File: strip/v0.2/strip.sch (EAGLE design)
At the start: 97 parts, among them IC1 LP2992, IC2 AUIRS2184S, IC3 MAX3051, IC5 AUIRS2184S, IC6 AUIRS2184S, IC7 STM32F050CX, Q1 IRF7828, Q2 IRF7828, Q3 IRF7828, Q4 IRF7828, Q5 IRF7828, Q6 IRF7828, U1 INA214AIDCKT

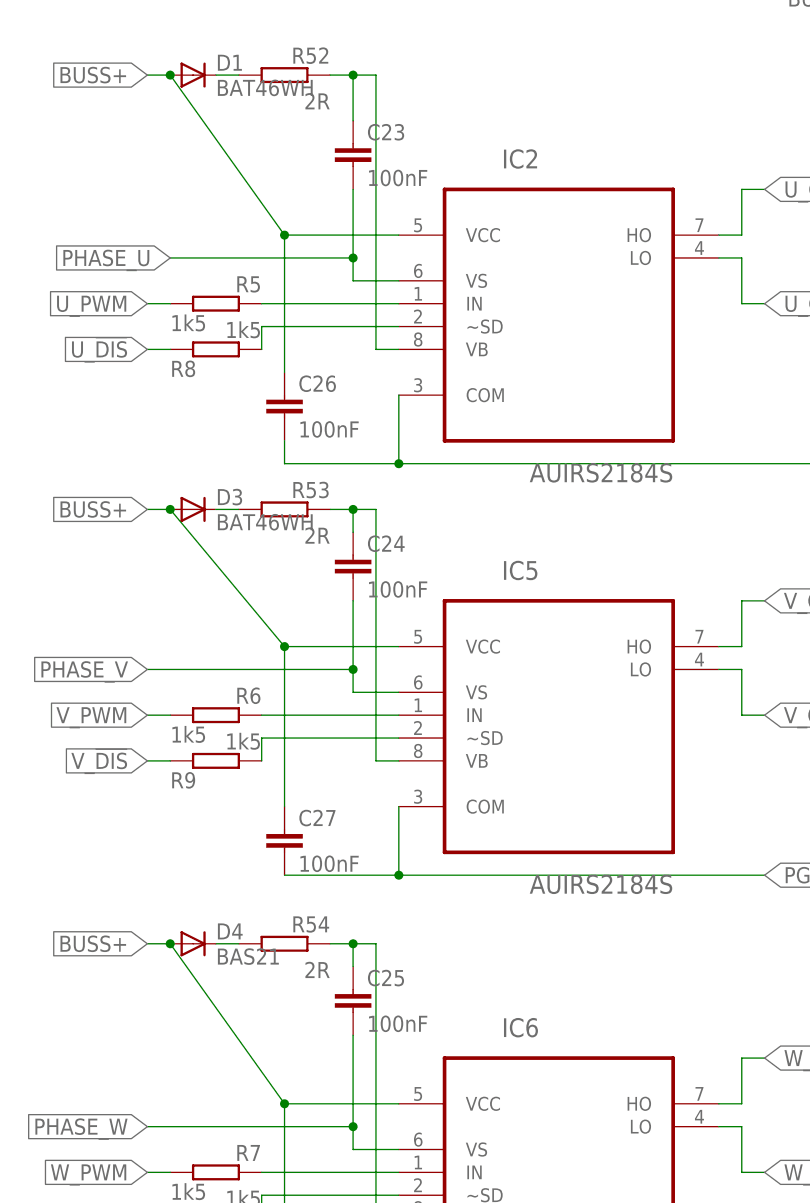
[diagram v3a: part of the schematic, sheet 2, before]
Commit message: Wired the layout of the new current measurement.
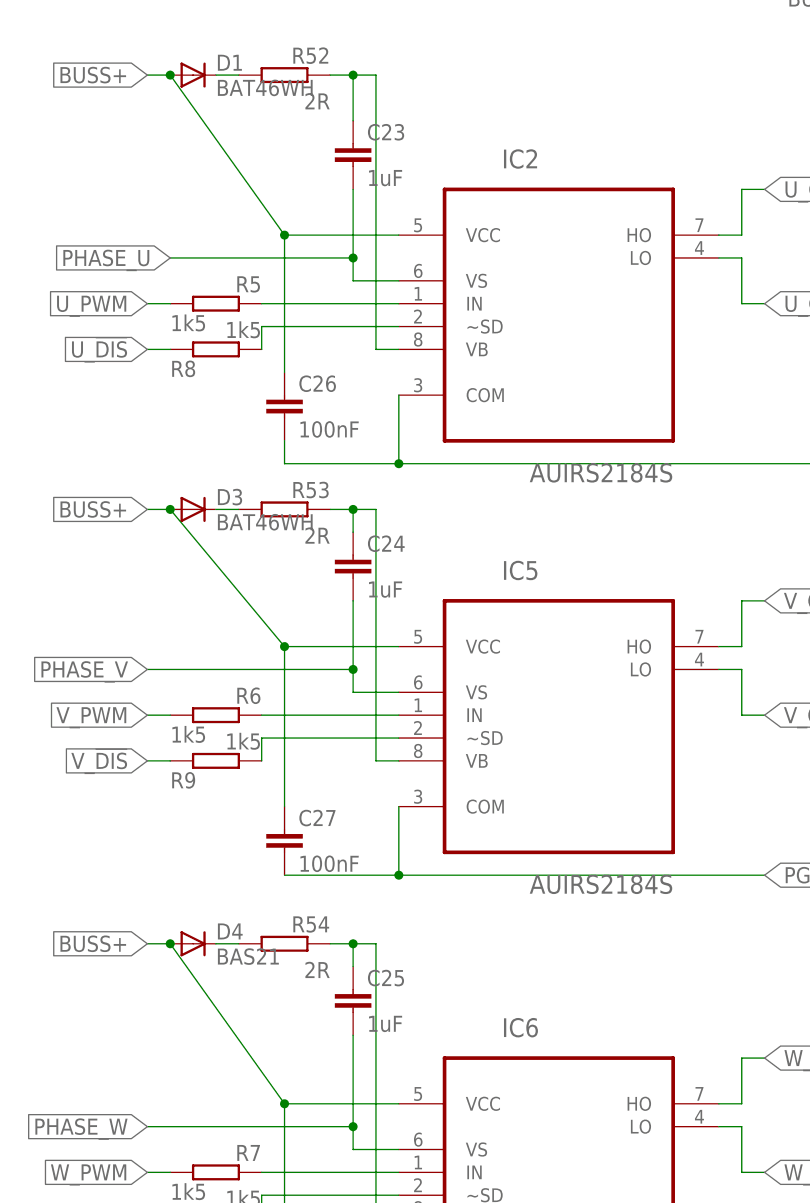
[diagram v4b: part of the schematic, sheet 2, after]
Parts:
- C1: value 4µ7 -> 1u; PARTNO cap-cer-0805-4u7-16v -> cap-cer-0805-1u-35v
- C23, C24, C25: value 100nF -> 1uF
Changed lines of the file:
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@@
 <grid distance="0.1" unitdist="inch" unit="inch" style="lines" multiple="1" display="no" altdistance="0.01" altunitdist="inch" altunit="inch"/>
 <layers>
-<layer number="1" name="Top" color="4" fill="1" visible="yes" active="no"/>
-<layer number="2" name="Route2" color="1" fill="3" visible="yes" active="no"/>
-<layer number="3" name="Route3" color="4" fill="3" visible="yes" active="no"/>
-<layer number="4" name="Route4" color="1" fill="4" visible="yes" active="no"/>
-<layer number="5" name="Route5" color="4" fill="4" visible="yes" active="no"/>
-<layer number="6" name="Route6" color="1" fill="8" visible="yes" active="no"/>
-<layer number="7" name="Route7" color="4" fill="8" visible="yes" active="no"/>
-<layer number="8" name="Route8" color="1" fill="2" visible="yes" active="no"/>
-<layer number="9" name="Route9" color="4" fill="2" visible="yes" active="no"/>
-<layer number="10" name="Route10" color="1" fill="7" visible="yes" active="no"/>
-<layer number="11" name="Route11" color="4" fill="7" visible="yes" active="no"/>
-<layer number="12" name="Route12" color="1" fill="5" visible="yes" active="no"/>
-<layer number="13" name="Route13" color="4" fill="5" visible="yes" active="no"/>
-<layer number="14" name="Route14" color="1" fill="6" visible="yes" active="no"/>
-<layer number="15" name="Route15" color="4" fill="6" visible="yes" active="no"/>
-<layer number="16" name="Bottom" color="1" fill="1" visible="yes" active="no"/>
-<layer number="17" name="Pads" color="2" fill="1" visible="yes" active="no"/>
-<layer number="18" name="Vias" color="2" fill="1" visible="yes" active="no"/>
-<layer number="19" name="Unrouted" color="6" fill="1" visible="yes" active="no"/>
-<layer number="20" name="Dimension" color="15" fill="1" visible="yes" active="no"/>
-<layer number="21" name="tPlace" color="7" fill="1" visible="yes" active="no"/>
-<layer number="22" name="bPlace" color="7" fill="1" visible="yes" active="no"/>
-<layer number="23" name="tOrigins" color="15" fill="1" visible="yes" active="no"/>
-<layer number="24" name="bOrigins" color="15" fill="1" visible="yes" active="no"/>
-<layer number="25" name="tNames" color="7" fill="1" visible="yes" active="no"/>
-<layer number="26" name="bNames" color="7" fill="1" visible="yes" active="no"/>
-<layer number="27" name="tValues" color="7" fill="1" visible="yes" active="no"/>
-<layer number="28" name="bValues" color="7" fill="1" visible="yes" active="no"/>
+<layer number="1" name="Top" color="4" fill="1" visible="no" active="no"/>
+<layer number="2" name="Route2" color="1" fill="3" visible="no" active="no"/>
+<layer number="3" name="Route3" color="4" fill="3" visible="no" active="no"/>
+<layer number="4" name="Route4" color="1" fill="4" visible="no" active="no"/>
+<layer number="5" name="Route5" color="4" fill="4" visible="no" active="no"/>
+<layer number="6" name="Route6" color="1" fill="8" visible="no" active="no"/>
+<layer number="7" name="Route7" color="4" fill="8" visible="no" active="no"/>
+<layer number="8" name="Route8" color="1" fill="2" visible="no" active="no"/>
+<layer number="9" name="Route9" color="4" fill="2" visible="no" active="no"/>
+<layer number="10" name="Route10" color="1" fill="7" visible="no" active="no"/>
+<layer number="11" name="Route11" color="4" fill="7" visible="no" active="no"/>
+<layer number="12" name="Route12" color="1" fill="5" visible="no" active="no"/>
+<layer number="13" name="Route13" color="4" fill="5" visible="no" active="no"/>
+<layer number="14" name="Route14" color="1" fill="6" visible="no" active="no"/>
+<layer number="15" name="Route15" color="4" fill="6" visible="no" active="no"/>
+<layer number="16" name="Bottom" color="1" fill="1" visible="no" active="no"/>
+<layer number="17" name="Pads" color="2" fill="1" visible="no" active="no"/>
+<layer number="18" name="Vias" color="2" fill="1" visible="no" active="no"/>
+<layer number="19" name="Unrouted" color="6" fill="1" visible="no" active="no"/>
+<layer number="20" name="Dimension" color="15" fill="1" visible="no" active="no"/>
+<layer number="21" name="tPlace" color="7" fill="1" visible="no" active="no"/>
+<layer number="22" name="bPlace" color="7" fill="1" visible="no" active="no"/>
+<layer number="23" name="tOrigins" color="15" fill="1" visible="no" active="no"/>
+<layer number="24" name="bOrigins" color="15" fill="1" visible="no" active="no"/>
+<layer number="25" name="tNames" color="7" fill="1" visible="no" active="no"/>
+<layer number="26" name="bNames" color="7" fill="1" visible="no" active="no"/>
+<layer number="27" name="tValues" color="7" fill="1" visible="no" active="no"/>
+<layer number="28" name="bValues" color="7" fill="1" visible="no" active="no"/>
 <layer number="29" name="tStop" color="7" fill="3" visible="no" active="no"/>
 <layer number="30" name="bStop" color="7" fill="6" visible="no" active="no"/>
@@
 <layer number="35" name="tGlue" color="7" fill="4" visible="no" active="no"/>
 <layer number="36" name="bGlue" color="7" fill="5" visible="no" active="no"/>
-<layer number="37" name="tTest" color="7" fill="1" visible="yes" active="no"/>
-<layer number="38" name="bTest" color="7" fill="1" visible="yes" active="no"/>
+<layer number="37" name="tTest" color="7" fill="1" visible="no" active="no"/>
+<layer number="38" name="bTest" color="7" fill="1" visible="no" active="no"/>
 <layer number="39" name="tKeepout" color="4" fill="11" visible="no" active="no"/>
 <layer number="40" name="bKeepout" color="1" fill="11" visible="no" active="no"/>
@@
 <layer number="44" name="Drills" color="7" fill="1" visible="no" active="no"/>
 <layer number="45" name="Holes" color="7" fill="1" visible="no" active="no"/>
-<layer number="46" name="Milling" color="3" fill="1" visible="yes" active="no"/>
-<layer number="47" name="Measures" color="7" fill="1" visible="yes" active="no"/>
-<layer number="48" name="Document" color="7" fill="1" visible="yes" active="no"/>
-<layer number="49" name="Reference" color="7" fill="1" visible="yes" active="no"/>
-<layer number="50" name="dxf" color="7" fill="1" visible="yes" active="no"/>
-<layer number="51" name="tDocu" color="7" fill="1" visible="yes" active="no"/>
-<layer number="52" name="bDocu" color="7" fill="1" visible="yes" active="no"/>
-<layer number="53" name="tGND_GNDA" color="7" fill="9" visible="yes" active="no"/>
-<layer number="54" name="bGND_GNDA" color="1" fill="9" visible="yes" active="no"/>
-<layer number="56" name="wert" color="7" fill="1" visible="yes" active="no"/>
-<layer number="59" name="Invisible" color="7" fill="1" visible="yes" active="no"/>
-<layer number="61" name="stand" color="7" fill="1" visible="yes" active="no"/>
+<layer number="46" name="Milling" color="3" fill="1" visible="no" active="no"/>
+<layer number="47" name="Measures" color="7" fill="1" visible="no" active="no"/>
+<layer number="48" name="Document" color="7" fill="1" visible="no" active="no"/>
+<layer number="49" name="Reference" color="7" fill="1" visible="no" active="no"/>
+<layer number="50" name="dxf" color="7" fill="1" visible="no" active="no"/>
+<layer number="51" name="tDocu" color="7" fill="1" visible="no" active="no"/>
+<layer number="52" name="bDocu" color="7" fill="1" visible="no" active="no"/>
+<layer number="53" name="tGND_GNDA" color="7" fill="9" visible="no" active="no"/>
+<layer number="54" name="bGND_GNDA" color="1" fill="9" visible="no" active="no"/>
+<layer number="56" name="wert" color="7" fill="1" visible="no" active="no"/>
+<layer number="59" name="Invisible" color="7" fill="1" visible="no" active="no"/>
+<layer number="61" name="stand" color="7" fill="1" visible="no" active="no"/>
 <layer number="91" name="Nets" color="2" fill="1" visible="yes" active="yes"/>
 <layer number="92" name="Busses" color="1" fill="1" visible="yes" active="yes"/>
@@
 </part>
 <part name="P+1" library="supply1" deviceset="+3V3" device=""/>
-<part name="C1" library="pel_dipol_comp" deviceset="CAPACITOR-POL" device="-0805" value="4µ7">
-<attribute name="PARTNO" value="cap-cer-0805-4u7-16v"/>
+<part name="C1" library="pel_dipol_comp" deviceset="CAPACITOR-POL" device="-0805" value="1u">
+<attribute name="PARTNO" value="cap-cer-0805-1u-35v"/>
 </part>
 <part name="P+29" library="supply1" deviceset="+3V3" device=""/>
@@
 <attribute name="PARTNO" value="*"/>
 </part>
-<part name="C23" library="pel_dipol_comp" deviceset="CAPACITOR" device="-0603" value="100nF">
+<part name="C23" library="pel_dipol_comp" deviceset="CAPACITOR" device="-0603" value="1uF">
 <attribute name="PARTNO" value="cap-tan-0603-1u"/>
 </part>
@@
 <attribute name="PARTNO" value="*"/>
 </part>
-<part name="C24" library="pel_dipol_comp" deviceset="CAPACITOR" device="-0603" value="100nF">
+<part name="C24" library="pel_dipol_comp" deviceset="CAPACITOR" device="-0603" value="1uF">
 <attribute name="PARTNO" value="cap-tan-0603-1u"/>
 </part>
@@
 <attribute name="PARTNO" value="*"/>
 </part>
-<part name="C25" library="pel_dipol_comp" deviceset="CAPACITOR" device="-0603" value="100nF">
+<part name="C25" library="pel_dipol_comp" deviceset="CAPACITOR" device="-0603" value="1uF">
 <attribute name="PARTNO" value="cap-tan-0603-1u"/>
 </part>

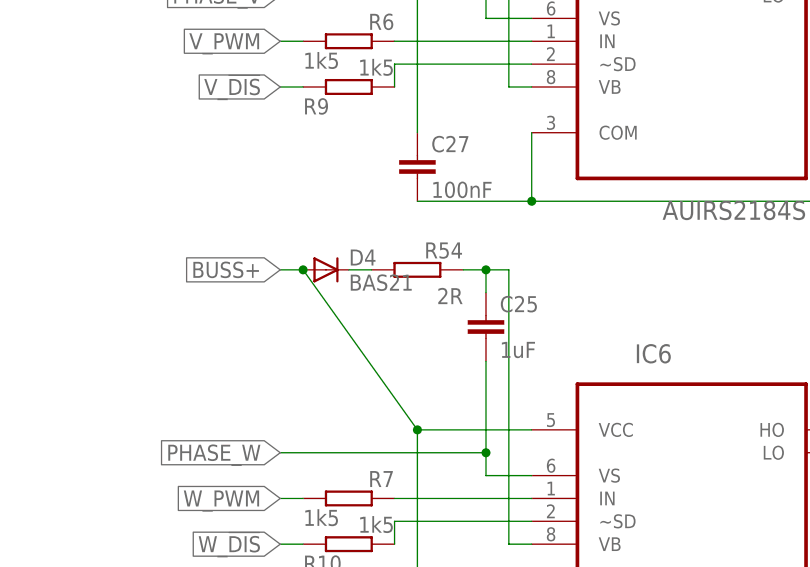
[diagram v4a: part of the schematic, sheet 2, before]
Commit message: Fixed some part descriptons.
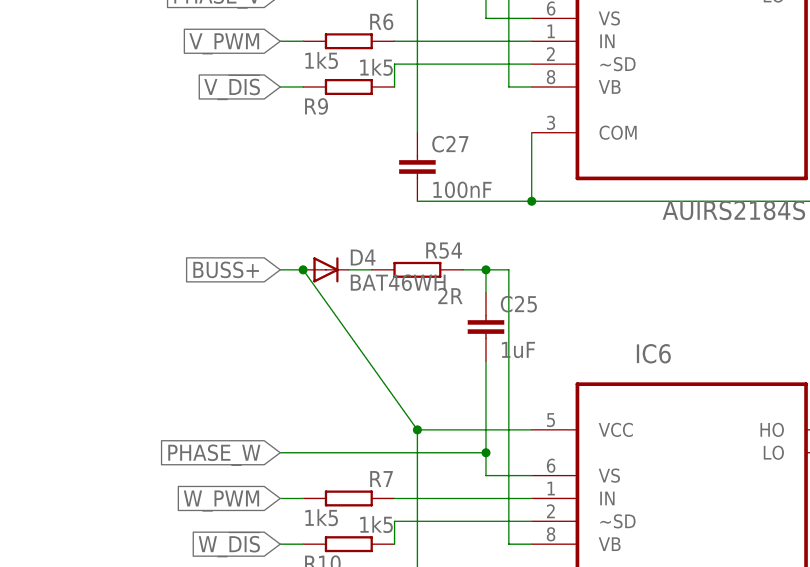
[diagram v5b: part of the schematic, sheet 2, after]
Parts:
- D4: value BAS21 -> BAT46WH
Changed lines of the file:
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@@
 <attribute name="PARTNO" value="cap-tan-0603-1u"/>
 </part>
-<part name="D4" library="pel_dipol_comp" deviceset="DIODE" device="-SOD-123" value="BAS21">
+<part name="D4" library="pel_dipol_comp" deviceset="DIODE" device="-SOD-123" value="BAT46WH">
 <attribute name="PARTNO" value="*"/>
 </part>

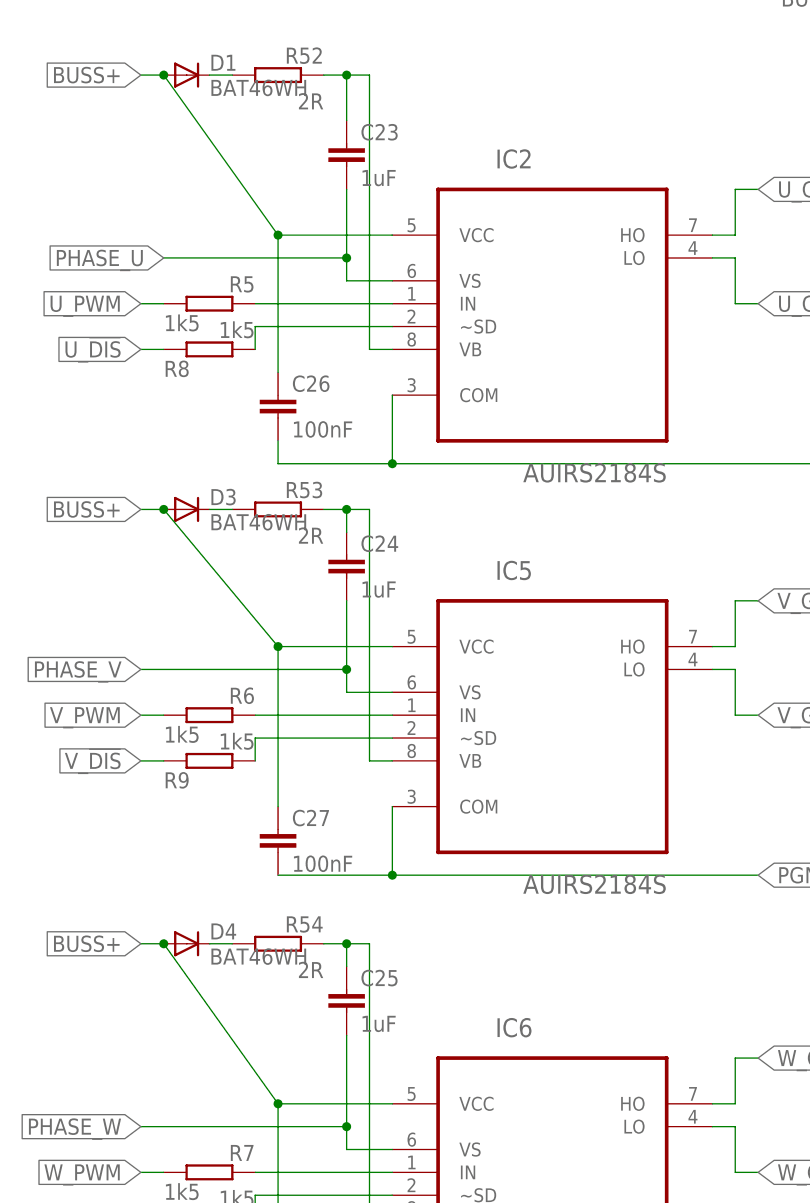
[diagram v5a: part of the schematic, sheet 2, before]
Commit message: Corrected some component values.
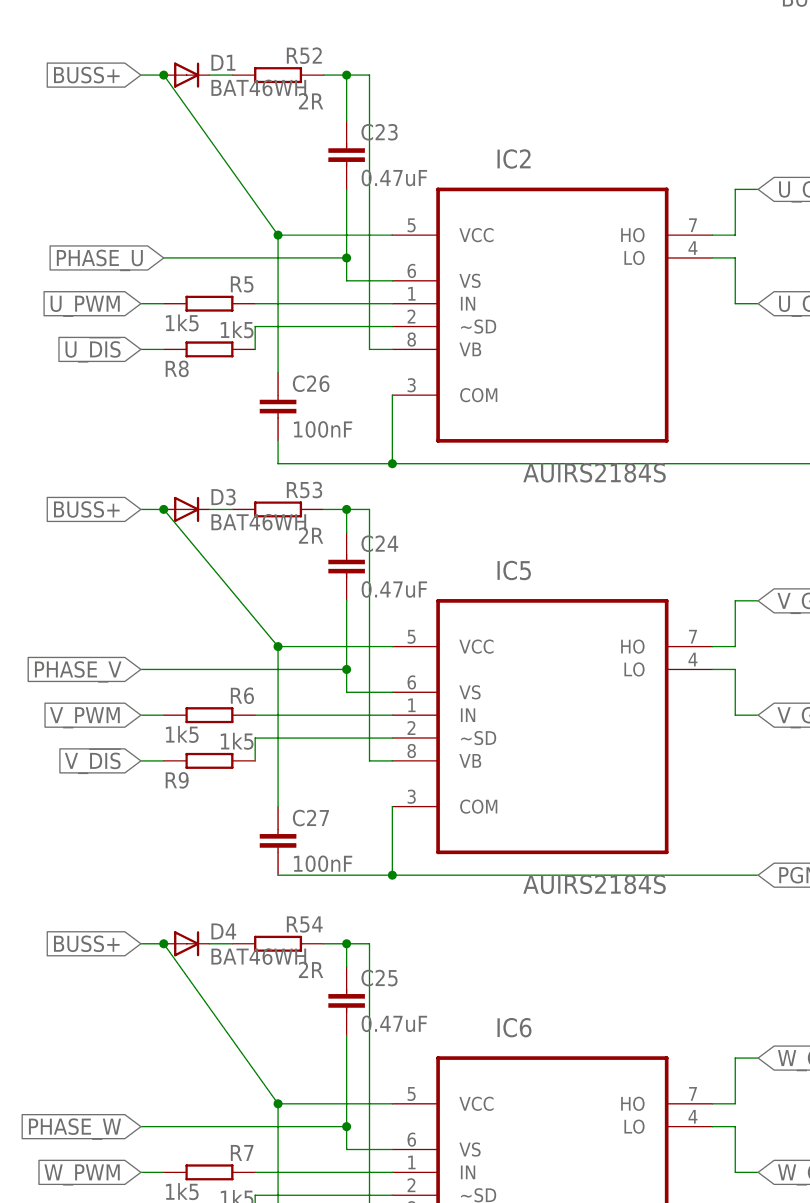
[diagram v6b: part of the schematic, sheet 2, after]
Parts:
- C23, C24, C25: value 1uF -> 0.47uF
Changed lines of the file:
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@@
 <attribute name="PARTNO" value="*"/>
 </part>
-<part name="C23" library="pel_dipol_comp" deviceset="CAPACITOR" device="-0603" value="1uF">
+<part name="C23" library="pel_dipol_comp" deviceset="CAPACITOR" device="-0603" value="0.47uF">
 <attribute name="PARTNO" value="cap-tan-0603-1u"/>
 </part>
@@
 <attribute name="PARTNO" value="*"/>
 </part>
-<part name="C24" library="pel_dipol_comp" deviceset="CAPACITOR" device="-0603" value="1uF">
+<part name="C24" library="pel_dipol_comp" deviceset="CAPACITOR" device="-0603" value="0.47uF">
 <attribute name="PARTNO" value="cap-tan-0603-1u"/>
 </part>
@@
 <attribute name="PARTNO" value="*"/>
 </part>
-<part name="C25" library="pel_dipol_comp" deviceset="CAPACITOR" device="-0603" value="1uF">
+<part name="C25" library="pel_dipol_comp" deviceset="CAPACITOR" device="-0603" value="0.47uF">
 <attribute name="PARTNO" value="cap-tan-0603-1u"/>
 </part>

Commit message: Pin COM of the IRS2184 driver is now connected to PGND... as it should.
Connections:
- net PGND: now also IC2.COM, IC5.COM, IC6.COM
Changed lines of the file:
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@@
 </segment>
 <segment>
-<wire x1="142.24" y1="147.32" x2="142.24" y2="154.94" width="0.1524" layer="91"/>
-<wire x1="142.24" y1="147.32" x2="190.5" y2="147.32" width="0.1524" layer="91"/>
+<wire x1="129.54" y1="147.32" x2="142.24" y2="147.32" width="0.1524" layer="91"/>
 <label x="190.5" y="147.32" size="1.778" layer="95" xref="yes"/>
 <pinref part="C26" gate="G$1" pin="2"/>
+<wire x1="142.24" y1="147.32" x2="190.5" y2="147.32" width="0.1524" layer="91"/>
 <wire x1="129.54" y1="149.86" x2="129.54" y2="147.32" width="0.1524" layer="91"/>
-<wire x1="129.54" y1="147.32" x2="142.24" y2="147.32" width="0.1524" layer="91"/>
+<pinref part="IC2" gate="A" pin="COM"/>
+<wire x1="142.24" y1="154.94" x2="142.24" y2="147.32" width="0.1524" layer="91"/>
 <junction x="142.24" y="147.32"/>
 </segment>
 <segment>
-<wire x1="142.24" y1="101.6" x2="142.24" y2="109.22" width="0.1524" layer="91"/>
-<wire x1="142.24" y1="101.6" x2="182.88" y2="101.6" width="0.1524" layer="91"/>
+<wire x1="129.54" y1="101.6" x2="142.24" y2="101.6" width="0.1524" layer="91"/>
 <label x="182.88" y="101.6" size="1.778" layer="95" xref="yes"/>
 <pinref part="C27" gate="G$1" pin="2"/>
-<wire x1="129.54" y1="101.6" x2="142.24" y2="101.6" width="0.1524" layer="91"/>
+<pinref part="IC5" gate="A" pin="COM"/>
+<wire x1="142.24" y1="101.6" x2="182.88" y2="101.6" width="0.1524" layer="91"/>
+<wire x1="142.24" y1="109.22" x2="142.24" y2="101.6" width="0.1524" layer="91"/>
 <junction x="142.24" y="101.6"/>
 </segment>
 <segment>
-<wire x1="142.24" y1="45.72" x2="142.24" y2="58.42" width="0.1524" layer="91"/>
-<wire x1="142.24" y1="45.72" x2="182.88" y2="45.72" width="0.1524" layer="91"/>
+<wire x1="129.54" y1="45.72" x2="142.24" y2="45.72" width="0.1524" layer="91"/>
 <label x="182.88" y="45.72" size="1.778" layer="95" xref="yes"/>
 <pinref part="C32" gate="G$1" pin="2"/>
+<wire x1="142.24" y1="45.72" x2="182.88" y2="45.72" width="0.1524" layer="91"/>
 <wire x1="129.54" y1="48.26" x2="129.54" y2="45.72" width="0.1524" layer="91"/>
-<wire x1="129.54" y1="45.72" x2="142.24" y2="45.72" width="0.1524" layer="91"/>
+<pinref part="IC6" gate="A" pin="COM"/>
+<wire x1="142.24" y1="58.42" x2="142.24" y2="45.72" width="0.1524" layer="91"/>
 <junction x="142.24" y="45.72"/>
 </segment>
